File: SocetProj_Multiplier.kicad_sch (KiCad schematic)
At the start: 0 parts

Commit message: added schematic for 8 bit inputs and their respective pulldownresistors. Added full adders and began addition module, needs to route outputs still
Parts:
- added J1: Barrel_Jack, symbol Connector:Barrel_Jack
- added R1, R10, R11, R12, R13, R14, R15, R16, R2, R3, R4, R5, R6, R7, R8, R9: 1k, symbol Device:R
- added U1, U2: 74LS283, symbol 74xx:74LS283
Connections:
- new net +5V: J1.1
- new net A0: R1.1, U1.5 (A1)
- new net A1: R2.1, U1.3 (A2)
- new net A2: R3.1, U1.14 (A3)
- new net A3: R4.1, U1.12 (A4)
- new net A4: R5.1, U2.5 (A1)
- new net A5: R6.1, U2.3 (A2)
- new net A6: R7.1, U2.14 (A3)
- new net A7: R8.1, U2.12 (A4)
- new net B0: R9.1, U1.6 (B1)
- new net B1: R10.1, U1.2 (B2)
- new net B2: R11.1, U1.15 (B3)
- new net B3: R12.1, U1.11 (B4)
- new net B4: R13.1, U2.6 (B1)
- new net B5: R14.1, U2.2 (B2)
- new net B6: R15.1, U2.15 (B3)
- new net B7: R16.1, U2.11 (B4)
- new net C_Out_1: U1.9 (C4), U2.7 (C0)
- new net GND: J1.2, R1.2, R10.2, R11.2, R12.2, R13.2, R14.2, R15.2, R16.2, R2.2, R3.2, R4.2, R5.2, R6.2, R7.2, R8.2, R9.2, U1.7 (C0), U1.8 (GND), U2.8 (GND)

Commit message: Added subtraction capabilities via Complement of 2 subtraction
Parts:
- added C1, C2: .1u, symbol Device:C
- added U4, U5: 74LS86, symbol 74xx:74LS86
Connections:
- net +5V: now also U1.16 (VCC), U2.16 (VCC), C1.1, C2.1
- net B0: now also U4.2; no longer U1.6 (B1)
- net B1: now also U4.5; no longer U1.2 (B2)
- net B2: now also U4.10; no longer U1.15 (B3)
- net B3: now also U4.13; no longer U1.11 (B4)
- net B4: now also U5.2; no longer U2.6 (B1)
- net B5: now also U5.5; no longer U2.2 (B2)
- net B6: now also U5.10; no longer U2.15 (B3)
- net B7: now also U5.13; no longer U2.11 (B4)
- net GND: now also C1.2, C2.2, U4.7 (GND), U5.7 (GND); no longer U1.7 (C0)
- new net C0: U1.7 (C0), U4.1, U4.12, U4.4, U4.9, U5.1, U5.12, U5.4, U5.9
- new net RA1: U1.6 (B1), U4.3
- new net RA2: U1.2 (B2), U4.6
- new net RA3: U1.15 (B3), U4.8
- new net RA4: U1.11 (B4), U4.11
- new net RB1: U2.6 (B1), U5.3
- new net RB2: U2.2 (B2), U5.6
- new net RB3: U2.15 (B3), U5.8
- new net RB4: U2.11 (B4), U5.11
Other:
- moved on the sheet: U1, U2

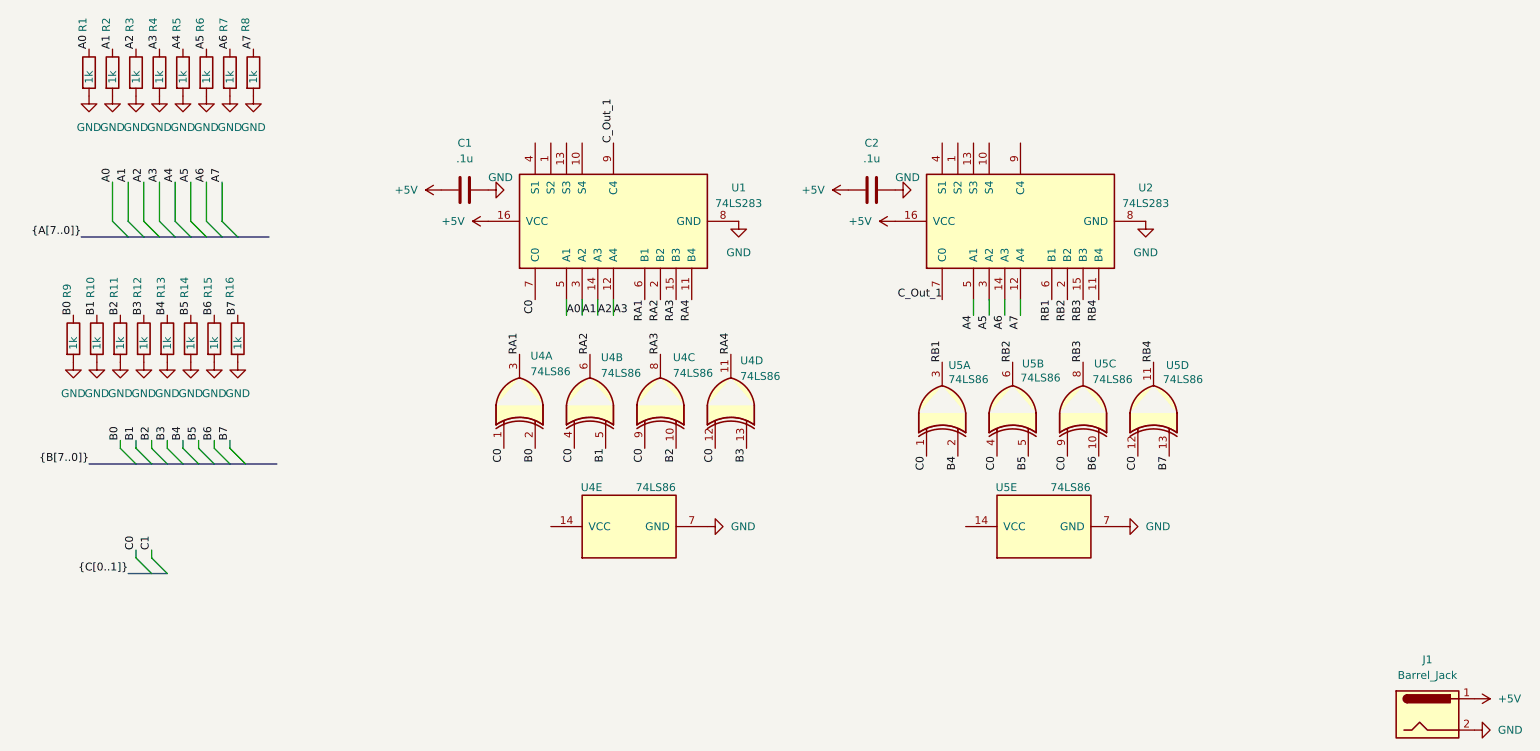
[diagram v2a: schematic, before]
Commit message: split components into seperate hierarchal modules with respective hierarchal tags. Need to figure out how to connect between modules still
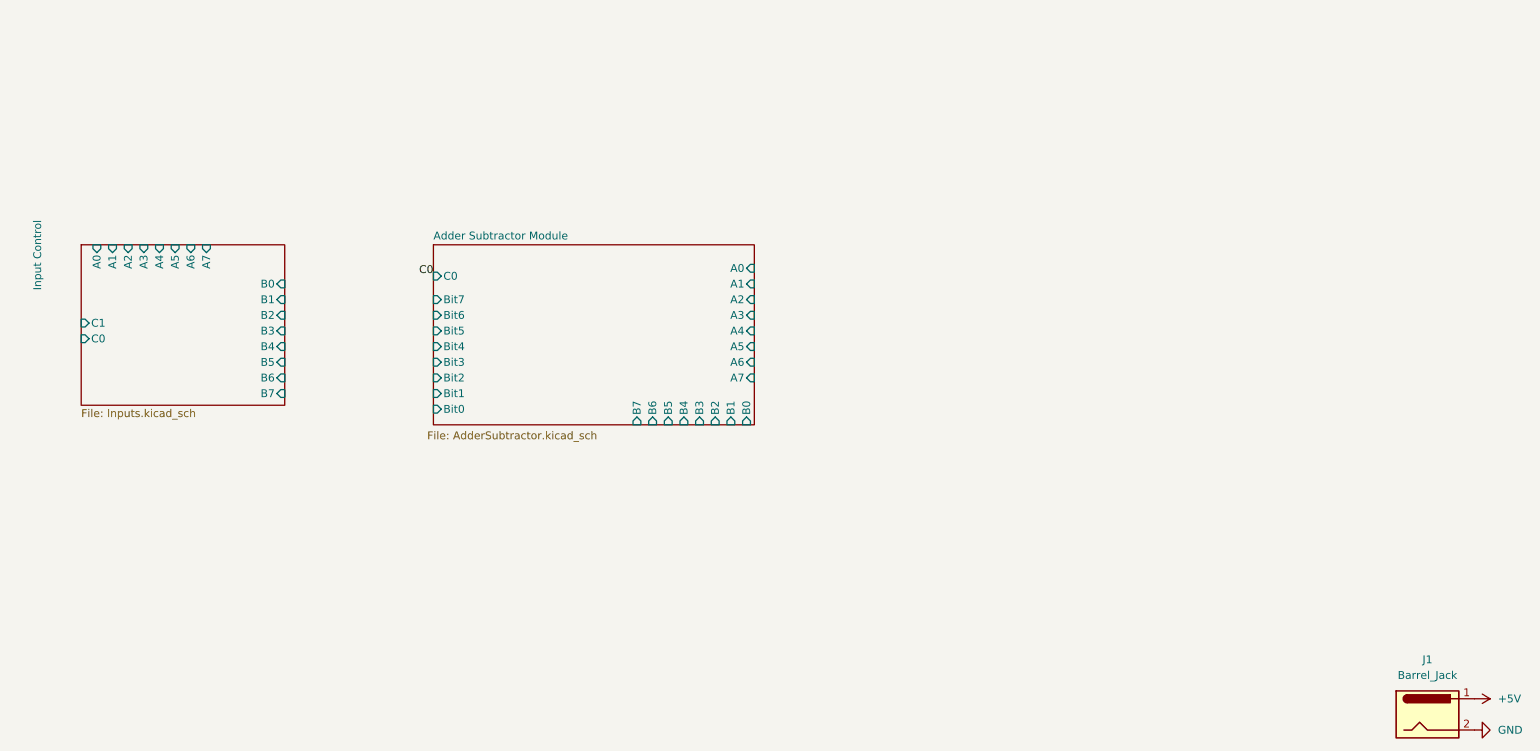
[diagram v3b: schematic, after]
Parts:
- removed C1, C2: .1u, symbol Device:C
- removed R1, R10, R11, R12, R13, R14, R15, R16, R2, R3, R4, R5, R6, R7, R8, R9: 1k, symbol Device:R
- removed U1, U2: 74LS283, symbol 74xx:74LS283
- removed U4, U5: 74LS86, symbol 74xx:74LS86
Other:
- added sheet Adder Subtractor Module (AdderSubtractor.kicad_sch)
- added sheet Input Control (Inputs.kicad_sch)
